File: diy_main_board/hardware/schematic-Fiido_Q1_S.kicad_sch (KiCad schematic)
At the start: 12 parts, among them J1 Connector_4, J2 Connector_2, U1 Step-down converter to 3.3V, U2 ESP32-S3-DevKitC

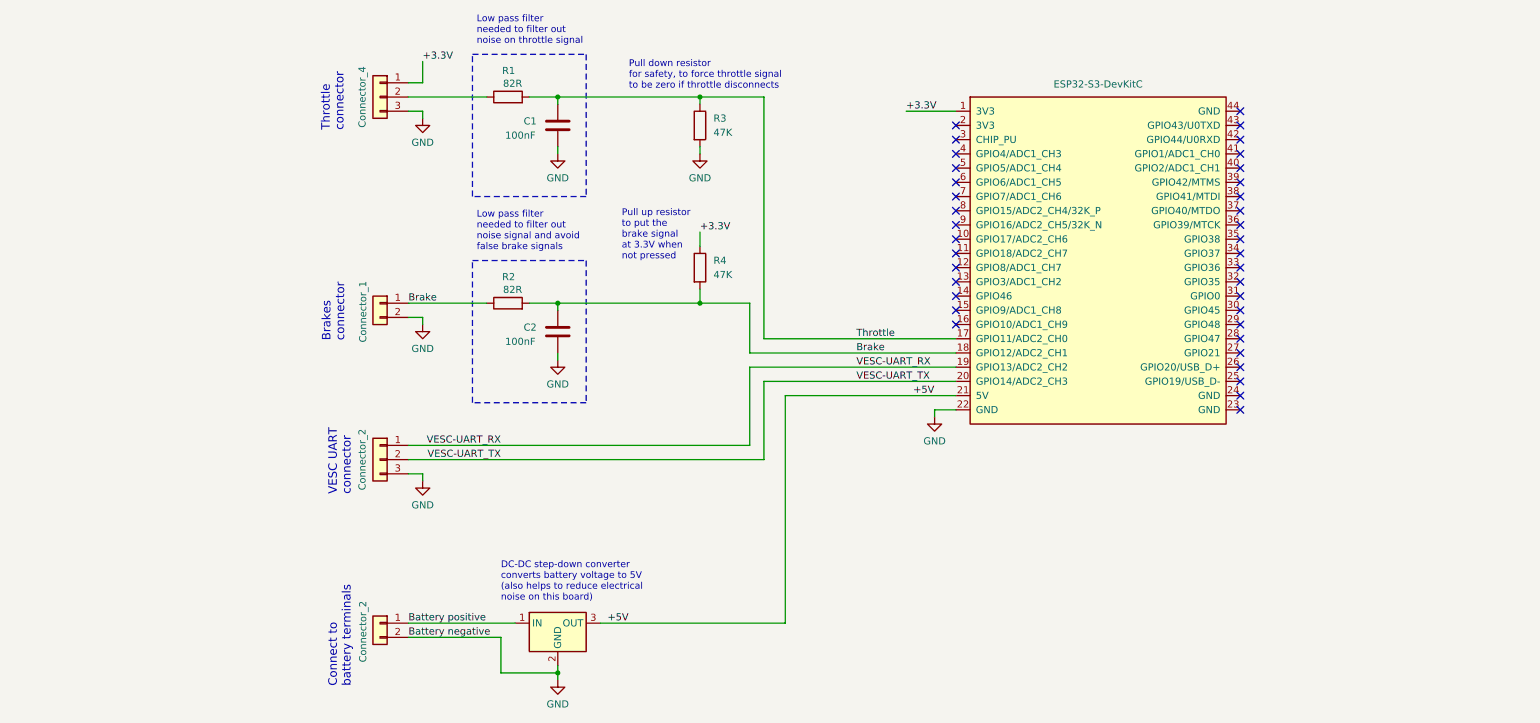
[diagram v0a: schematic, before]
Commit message: Changed motor main board to use ESP32-C3 instead of ESP32-S3
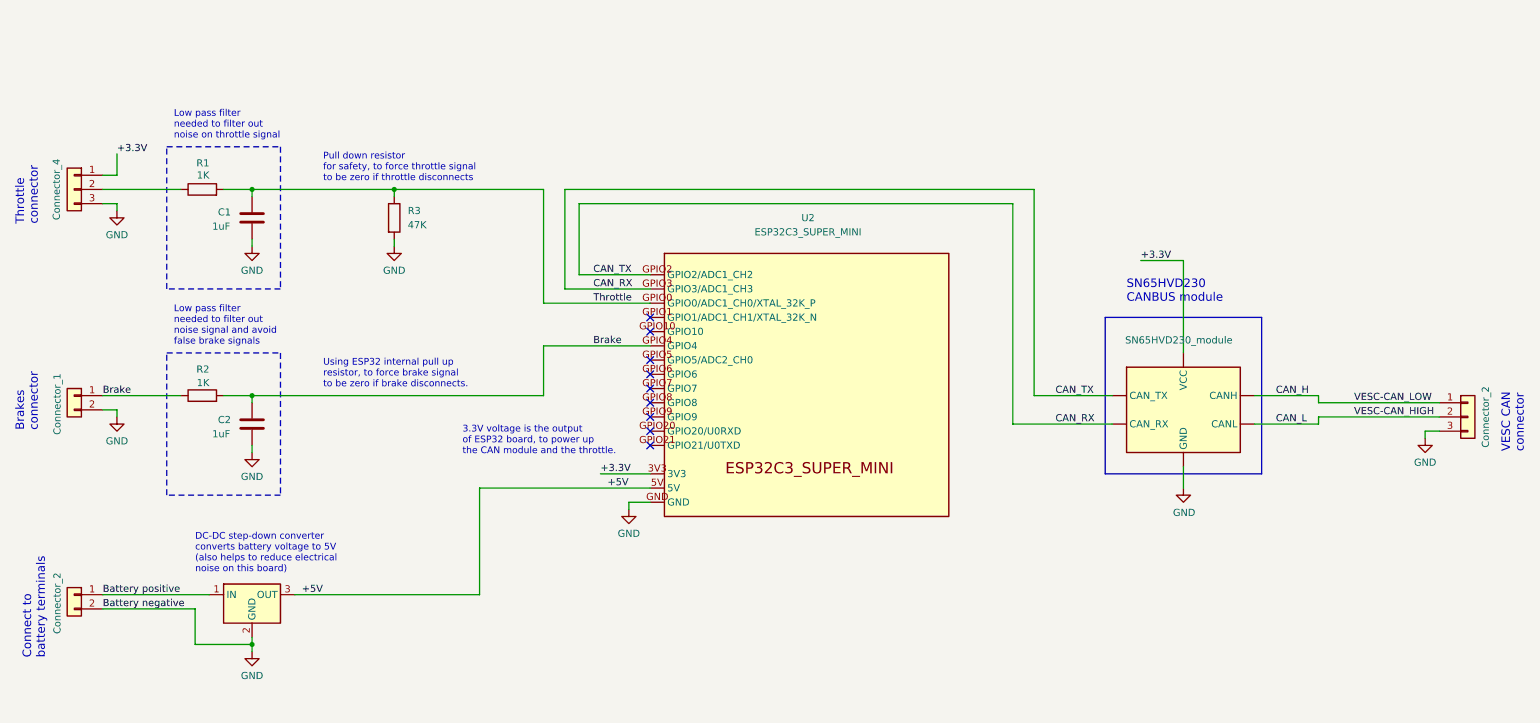
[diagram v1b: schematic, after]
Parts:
- removed R4: 47K, symbol Device:R
- removed U2: ESP32-S3-DevKitC, Espressif:ESP32-S3-DevKitC, symbol Espressif:ESP32-S3-DevKitC
- added U2: ESP32C3_SUPER_MINI, symbol Espressif:ESP32-C3-MINI-1
- added U3: SN65HVD230_module, symbol TJA1050:TJA1050_module
- C1, C2: value 100nF -> 1uF
- R1, R2: value 82R -> 1K
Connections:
- net +3.3V: now also U2.3V3, U3. (CANL)
- net +5V: now also U2.5V
- net Brake: now also U2.GPIO4
- net GND: now also U2.GND, U3. (CANL)
- net Throttle: now also U2.GPIO0 (GPIO0/ADC1_CH0/XTAL_32K_P)
- net VESC-UART_RX renamed CAN_H
- net CAN_H: now also U3. (CANL)
- net VESC-UART_TX renamed CAN_L
- net CAN_L: now also U3. (CANL)
- new net CAN_RX: U2.GPIO2 (GPIO2/ADC1_CH2), U2.GPIO3 (GPIO3/ADC1_CH3), U3. (CANL)
- no-connect marks 37 -> 9
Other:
- note added: "3.3V voltage is the output of ESP32 board, to power up the CAN module and the throttle."
- note added: "SN65HVD230 CANBUS module"
- note added: "Using ESP32 internal pull up resistor, to force brake signal to be zero if brake disconnects."
- note added: "VESC CAN connector"
- note removed: "Pull up resistor to put the brake signal at 3.3V when not pressed"
- note removed: "VESC UART connector"
- moved on the sheet: C1, C2, Connector_1, Connector_2, R1, R2
